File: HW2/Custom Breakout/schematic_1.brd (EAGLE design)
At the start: 50 x 50 mm, 22 parts, among them J1 USB-MB-H

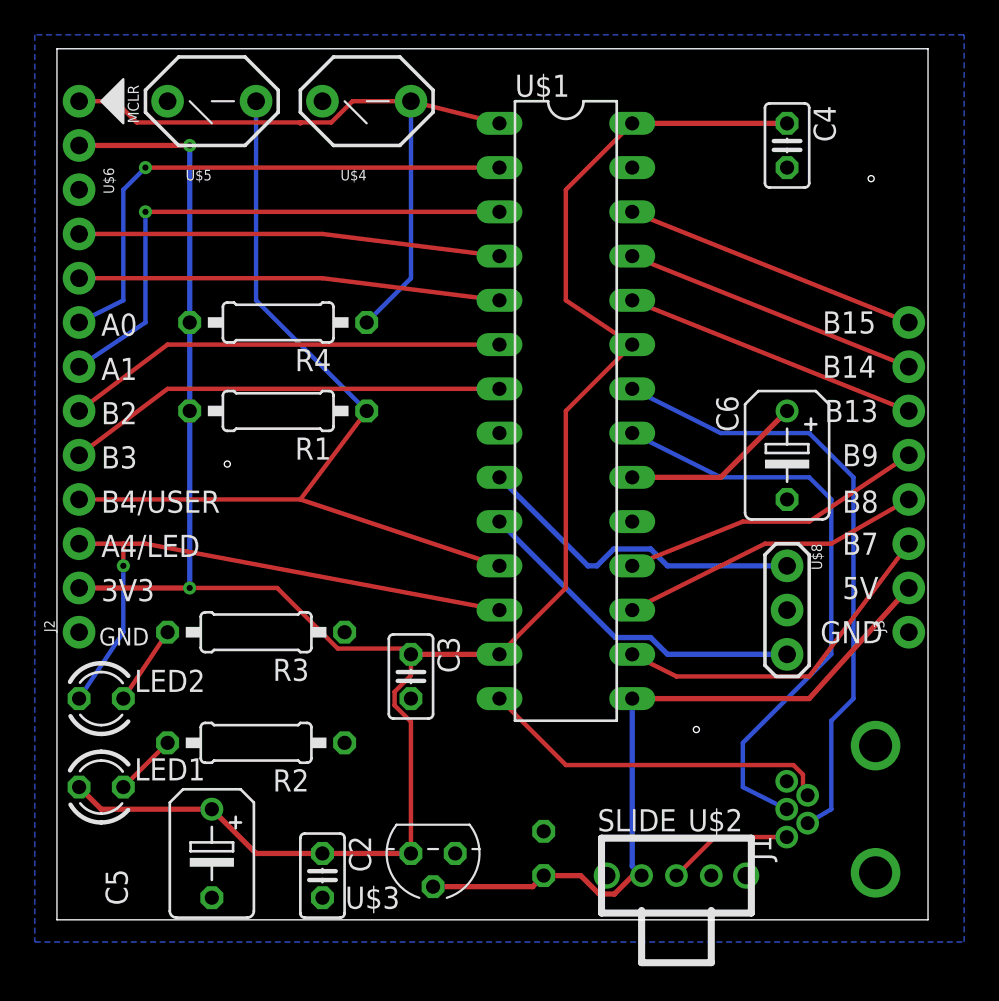
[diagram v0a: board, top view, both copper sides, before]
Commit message: Final adjustments, moved the new gerber files into the HW directory. Never figured out why some of the silkscreen for the parts shows up on the bottom. Ignoring that for now.
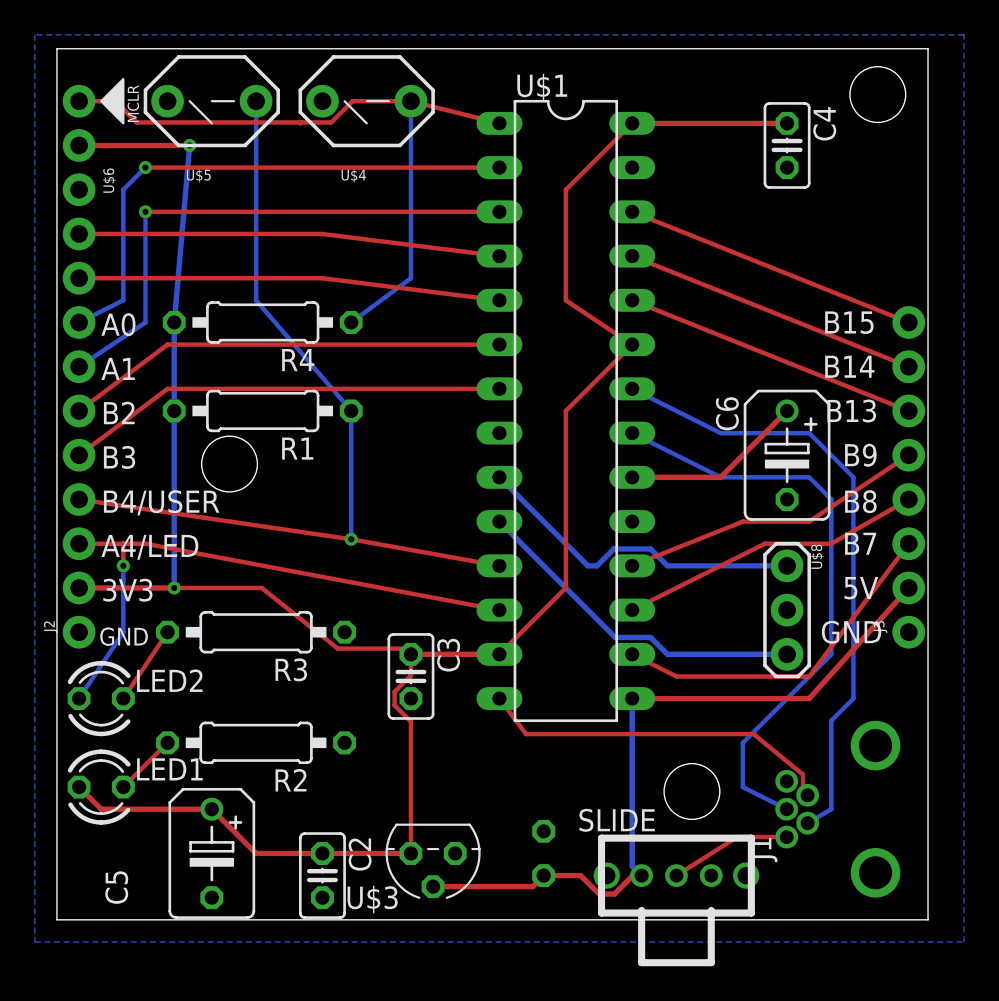
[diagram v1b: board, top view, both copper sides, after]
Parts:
- moved R1 0.89 mm to (11.8, 29.2)
- moved R4 0.89 mm to (11.8, 34.3)
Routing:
- net MCLR: track 39.1 -> 39.8 mm
- net B4/USER: track 51.5 -> 51.6 mm, vias 0 -> 1
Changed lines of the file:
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@@
 <layer number="20" name="Dimension" color="24" fill="1" visible="yes" active="yes"/>
 <layer number="21" name="tPlace" color="7" fill="1" visible="yes" active="yes"/>
-<layer number="22" name="bPlace" color="7" fill="1" visible="yes" active="yes"/>
+<layer number="22" name="bPlace" color="7" fill="1" visible="no" active="yes"/>
 <layer number="23" name="tOrigins" color="15" fill="1" visible="yes" active="yes"/>
 <layer number="24" name="bOrigins" color="15" fill="1" visible="yes" active="yes"/>
@@
 <text x="47.244" y="31.115" size="1.27" layer="22" rot="MR0">B14</text>
 <text x="47.244" y="33.655" size="1.27" layer="22" rot="MR0">B15</text>
-<hole x="46.736" y="42.545" drill="0.35"/>
-<hole x="9.779" y="26.162" drill="0.35"/>
-<hole x="36.703" y="10.922" drill="0.35"/>
 <rectangle x1="24.592" y1="3.962" x2="24.672" y2="4.002" layer="22"/>
 <rectangle x1="24.592" y1="4.002" x2="24.672" y2="4.042" layer="22"/>
@@
 <rectangle x1="43.712" y1="43.202" x2="43.792" y2="43.242" layer="22"/>
 <rectangle x1="43.752" y1="43.242" x2="43.832" y2="43.282" layer="22"/>
+<hole x="47.117" y="47.371" drill="3.2"/>
+<hole x="36.449" y="7.366" drill="3.2"/>
+<hole x="9.906" y="26.162" drill="3.2"/>
 </plain>
 <attributes>
@@
 <element name="LED1" library="custom" package="LED3MM" package3d_urn="urn:adsk.eagle:package:15797/1" value="RED" x="2.54" y="7.62"/>
 <element name="LED2" library="custom" package="LED3MM" package3d_urn="urn:adsk.eagle:package:15797/1" value="GREEN" x="2.54" y="12.7"/>
-<element name="R1" library="custom" package="0207/10" package3d_urn="urn:adsk.eagle:package:25939/1" value="10k" x="12.7" y="29.21" rot="R180"/>
+<element name="R1" library="custom" package="0207/10" package3d_urn="urn:adsk.eagle:package:25939/1" value="10k" x="11.811" y="29.21" rot="R180"/>
 <element name="R2" library="custom" package="0207/10" package3d_urn="urn:adsk.eagle:package:25939/1" value="330" x="11.43" y="10.16" rot="R180"/>
 <element name="R3" library="custom" package="0207/10" package3d_urn="urn:adsk.eagle:package:25939/1" value="330" x="11.43" y="16.51" rot="R180"/>
-<element name="R4" library="custom" package="0207/10" package3d_urn="urn:adsk.eagle:package:25939/1" value="10k" x="12.7" y="34.29" rot="R180"/>
+<element name="R4" library="custom" package="0207/10" package3d_urn="urn:adsk.eagle:package:25939/1" value="10k" x="11.811" y="34.29" rot="R180"/>
 <element name="U$1" library="custom" package="DIL28-3" package3d_urn="urn:adsk.eagle:package:14453/1" value="PIC32MX250F128B" x="29.21" y="29.21" rot="R270"/>
 <element name="U$2" library="custom" package="SLIDE" value="SLIDE" x="35.56" y="2.54" smashed="yes" rot="R180">
-<attribute name="NAME" x="39.37" y="6.35" size="1.27" layer="21" rot="R180"/>
-<attribute name="VALUE" x="35.56" y="6.35" size="1.27" layer="21" rot="R180"/>
+<attribute name="VALUE" x="34.417" y="6.35" size="1.27" layer="21" rot="R180"/>
 </element>
 <element name="U$3" library="custom" package="TO92" value="MCP1702" x="21.59" y="3.81" smashed="yes" rot="R180">
@@
 <contactref element="J1" pad="VBUS"/>
 <contactref element="U$2" pad="2"/>
-<wire x1="41.89" y1="4.75" x2="37.77" y2="4.75" width="0.254" layer="1"/>
-<wire x1="37.77" y1="4.75" x2="35.56" y2="2.54" width="0.254" layer="1"/>
+<wire x1="41.89" y1="4.75" x2="39.04" y2="4.75" width="0.254" layer="1"/>
+<wire x1="39.04" y1="4.75" x2="35.56" y2="2.54" width="0.254" layer="1"/>
 </signal>
 <signal name="+5V">
@@
 <wire x1="8.89" y1="6.35" x2="2.54" y2="6.35" width="0.3048" layer="1"/>
 <wire x1="2.54" y1="6.35" x2="1.27" y2="7.62" width="0.3048" layer="1"/>
-<wire x1="7.62" y1="34.29" x2="7.62" y2="29.21" width="0.3048" layer="16"/>
-<wire x1="7.62" y1="29.21" x2="7.62" y2="19.05" width="0.3048" layer="16"/>
-<via x="7.62" y="19.05" extent="1-16" drill="0.35"/>
-<wire x1="7.62" y1="19.05" x2="1.27" y2="19.05" width="0.3048" layer="1"/>
-<wire x1="7.62" y1="34.29" x2="7.62" y2="44.45" width="0.3048" layer="16"/>
+<wire x1="6.731" y1="34.29" x2="6.731" y2="29.21" width="0.3048" layer="16"/>
+<wire x1="6.731" y1="29.21" x2="6.731" y2="19.05" width="0.3048" layer="16"/>
+<via x="6.731" y="19.05" extent="1-16" drill="0.35"/>
+<wire x1="6.731" y1="19.05" x2="1.27" y2="19.05" width="0.3048" layer="1"/>
+<wire x1="6.731" y1="34.29" x2="7.62" y2="44.45" width="0.3048" layer="16"/>
 <via x="7.62" y="44.45" extent="1-16" drill="0.35"/>
 <wire x1="7.62" y1="44.45" x2="1.27" y2="44.45" width="0.3048" layer="1"/>
@@
 <wire x1="19.3802" y1="13.08928125" x2="20.32" y2="14.02908125" width="0.254" layer="1"/>
 <wire x1="20.32" y1="15.24" x2="19.9898" y2="15.5702" width="0.254" layer="1"/>
-<wire x1="12.64091875" y1="19.05" x2="7.62" y2="19.05" width="0.254" layer="1"/>
+<wire x1="11.75191875" y1="19.05" x2="6.731" y2="19.05" width="0.254" layer="1"/>
 <wire x1="19.9898" y1="15.5702" x2="16.12071875" y2="15.5702" width="0.254" layer="1"/>
-<wire x1="16.12071875" y1="15.5702" x2="12.64091875" y2="19.05" width="0.254" layer="1"/>
+<wire x1="16.12071875" y1="15.5702" x2="11.75191875" y2="19.05" width="0.254" layer="1"/>
 </signal>
 <signal name="N$8">
@@
 <contactref element="R4" pad="1"/>
 <contactref element="U$4" pad="1"/>
-<wire x1="17.78" y1="34.29" x2="20.32" y2="36.83" width="0.254" layer="16"/>
+<wire x1="16.891" y1="34.29" x2="20.32" y2="36.83" width="0.254" layer="16"/>
 <wire x1="20.32" y1="36.83" x2="20.32" y2="46.99" width="0.254" layer="16"/>
 <wire x1="25.4" y1="45.72" x2="20.32" y2="46.99" width="0.254" layer="1"/>
@@
 <contactref element="U$5" pad="1"/>
 <contactref element="J2" pad="4"/>
-<wire x1="1.27" y1="24.13" x2="13.97" y2="24.13" width="0.254" layer="1"/>
-<wire x1="13.97" y1="24.13" x2="25.4" y2="20.32" width="0.254" layer="1"/>
-<wire x1="13.97" y1="24.13" x2="17.78" y2="29.21" width="0.254" layer="1"/>
-<wire x1="17.78" y1="29.21" x2="11.43" y2="35.56" width="0.254" layer="16"/>
+<wire x1="16.891" y1="29.21" x2="11.43" y2="35.56" width="0.254" layer="16"/>
 <wire x1="11.43" y1="35.56" x2="11.43" y2="46.99" width="0.254" layer="16"/>
+<wire x1="25.4" y1="20.32" x2="16.891" y2="21.844" width="0.254" layer="1"/>
+<via x="16.891" y="21.844" extent="1-16" drill="0.35"/>
+<wire x1="16.891" y1="21.844" x2="16.891" y2="29.21" width="0.254" layer="16"/>
+<wire x1="1.27" y1="24.13" x2="16.891" y2="21.844" width="0.254" layer="1"/>
 </signal>
 <signal name="A4/LED">
@@
 <contactref element="U$1" pad="14"/>
 <contactref element="J1" pad="ID"/>
-<wire x1="42.8234" y1="8.33663125" x2="42.27663125" y2="8.8834" width="0.254" layer="1"/>
+<wire x1="42.8234" y1="8.33663125" x2="39.99063125" y2="10.6614" width="0.254" layer="1"/>
 <wire x1="43.09" y1="7.15" x2="42.8234" y2="7.4166" width="0.254" layer="1"/>
 <wire x1="42.8234" y1="7.4166" x2="42.8234" y2="8.33663125" width="0.254" layer="1"/>
-<wire x1="29.2166" y1="8.8834" x2="25.4" y2="12.7" width="0.254" layer="1"/>
-<wire x1="42.27663125" y1="8.8834" x2="29.2166" y2="8.8834" width="0.254" layer="1"/>
+<wire x1="26.9306" y1="10.6614" x2="25.4" y2="12.7" width="0.254" layer="1"/>
+<wire x1="39.99063125" y1="10.6614" x2="26.9306" y2="10.6614" width="0.254" layer="1"/>
 </signal>
 <signal name="OSC2">
@@
 </signal>
 </signals>
+<errors>
+</errors>
 </board>
 </drawing>
